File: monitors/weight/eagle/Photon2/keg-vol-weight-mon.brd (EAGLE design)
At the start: 92.5 x 52.9 mm, 18 parts, among them U1 PHOTON2

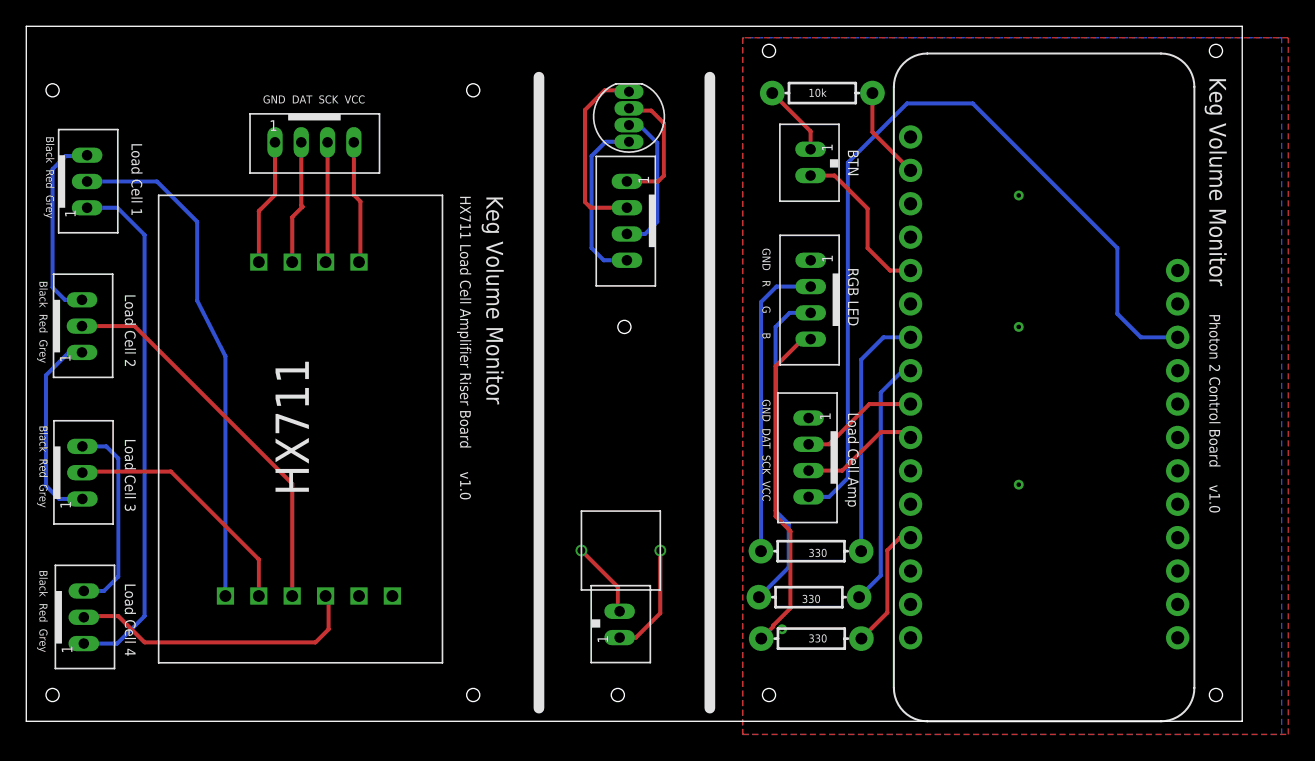
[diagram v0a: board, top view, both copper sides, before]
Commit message: Got the device registration process working
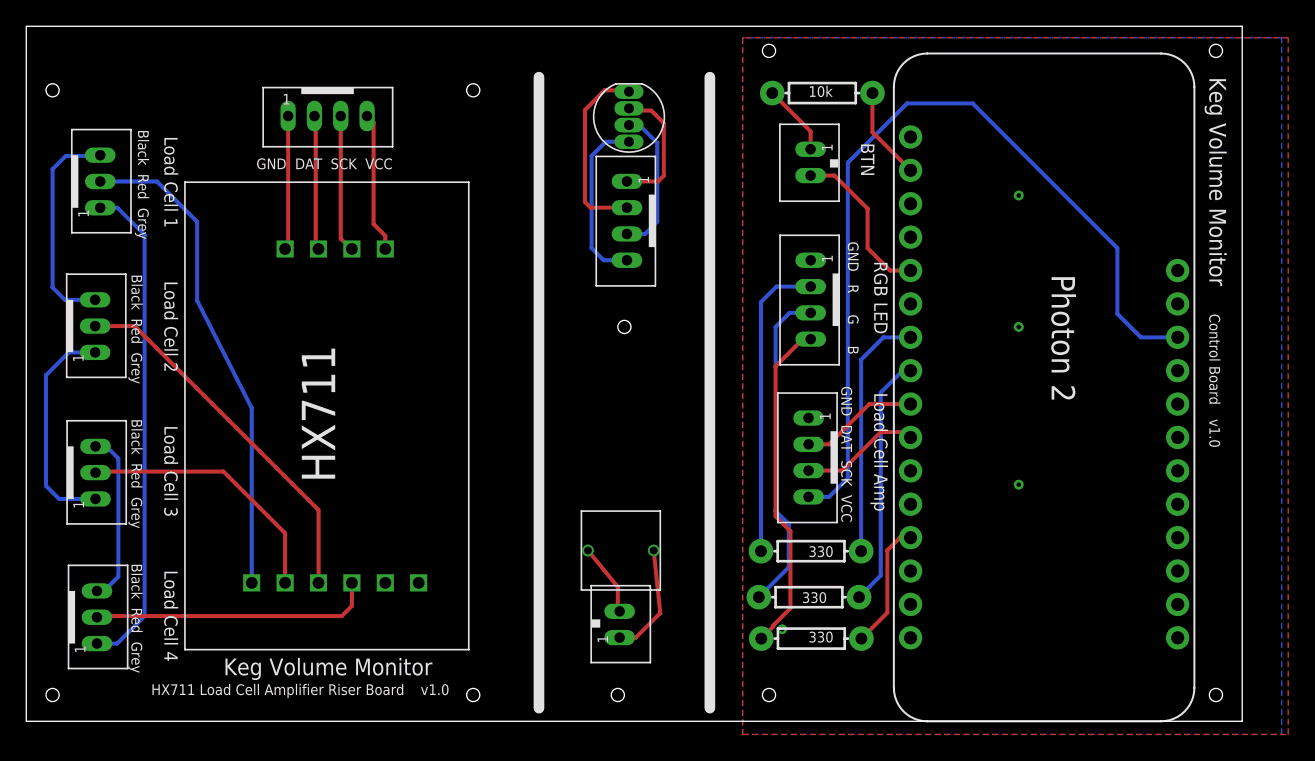
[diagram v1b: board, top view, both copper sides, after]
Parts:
- R1, R2, R3: value 330 -> (none)
- R4: value 10k -> (none)
- moved U$6 2.24 mm to (22.9, 46.1)
- moved U$4 2.24 mm to (33.7, 5.45)
- moved U$10 1.00 mm to (5.33, 7.94)
- moved U$7 1.00 mm to (5.58, 41.1)
- moved U$8 1.00 mm to (5.19, 30.1)
- moved U$9 1.00 mm to (5.22, 18.9)
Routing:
- net N$15: track 39.7 -> 37.7 mm
- net N$14: track 15.2 -> 13.2 mm
- net N$13: track 15.1 -> 17.1 mm
- net N$12: track 14.7 -> 16.7 mm
- net N$5: track 38.6 -> 37.1 mm
- net N$19: track 9.37 -> 10.7 mm
- net N$18: track 9.18 -> 10.5 mm
- net N$11: track 22.7 -> 21.5 mm
- net N$9: track 29.5 -> 28.3 mm
- net N$10: track 19.0 -> 20.2 mm
- net N$17: track 9.48 -> 10.2 mm
- net N$16: track 9.62 -> 10.2 mm
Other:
- board text added: "Control Board"
- board text added: "Photon 2"
- board text removed: "Photon 2 Control Board"
